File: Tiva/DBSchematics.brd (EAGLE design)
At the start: 125 x 84.1 mm, 68 parts, among them IC1 LM1117-3.3, IC2 7805T, IC3 MCP23017SO, Q1 BSS138, Q2 BSS138, U1 FT232RL, U2 LMV358, U3 LMV324, Y1 16MHz, Y2 32.768kHz

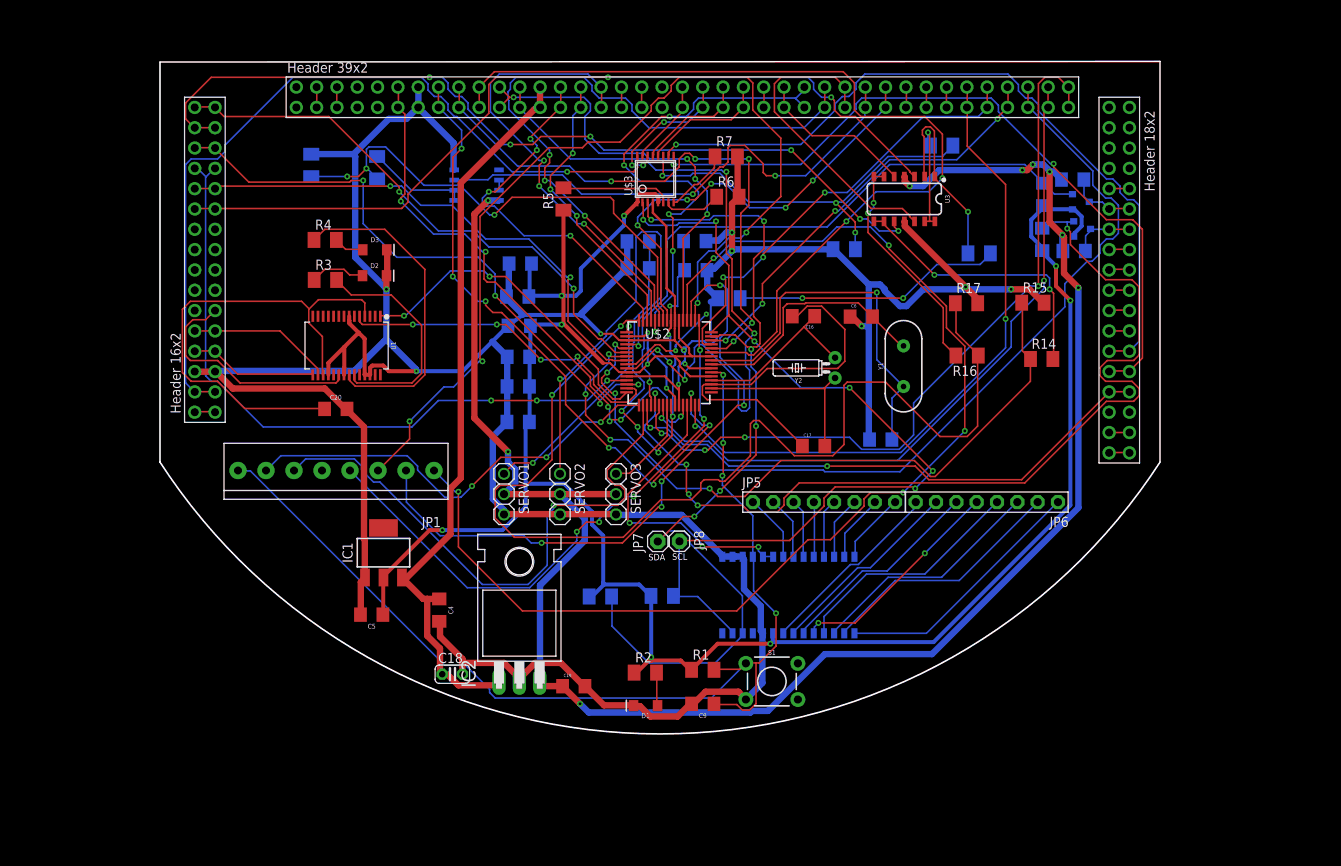
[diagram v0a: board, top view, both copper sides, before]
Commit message: uC based Board with manual Routing
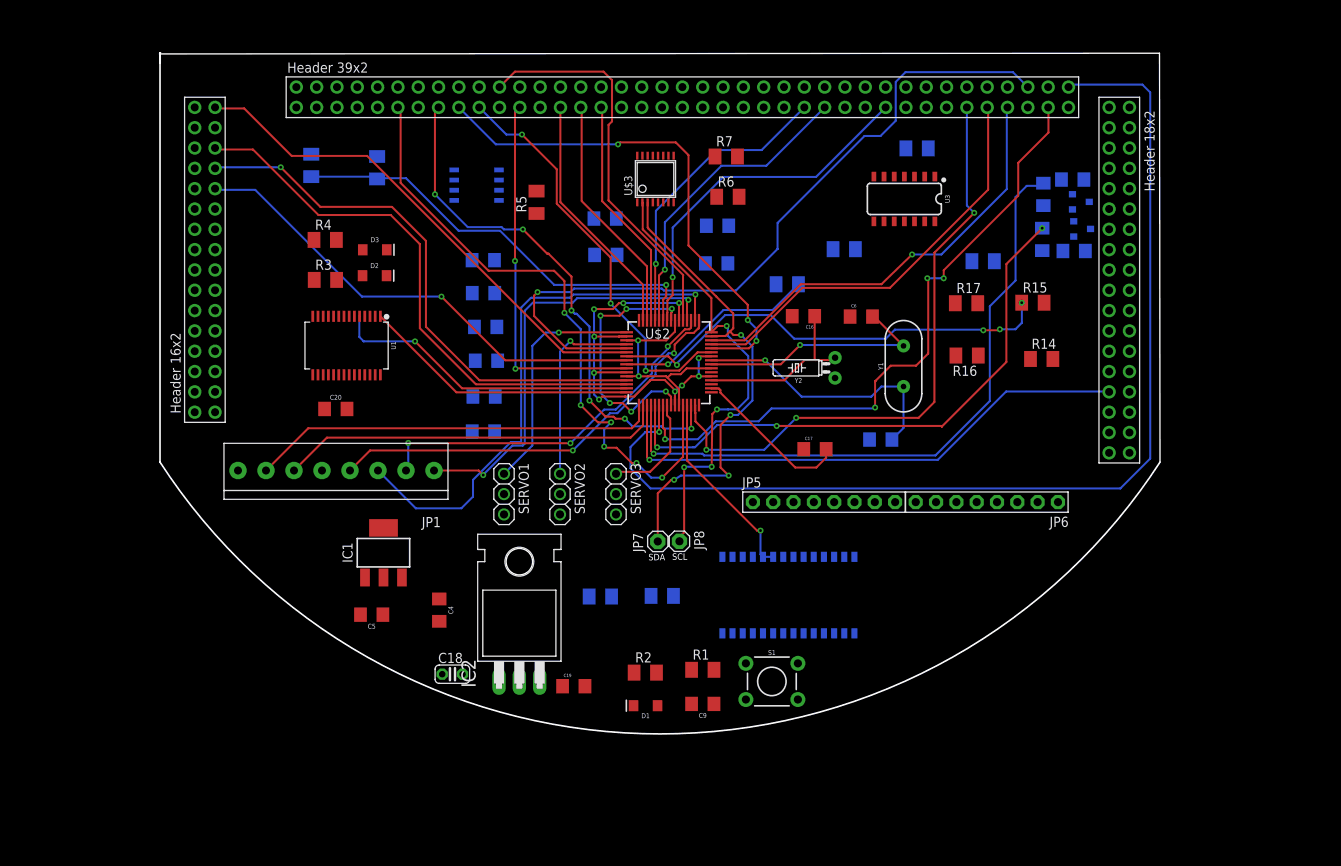
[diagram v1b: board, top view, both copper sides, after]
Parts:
- moved R13 7.50 mm to (78.4, 22.2)
- moved C1 5.02 mm to (55.6, 30.4)
- moved C11 4.64 mm to (40.4, 25.2)
- moved C8 4.50 mm to (40.4, 3.83)
- moved C14 4.45 mm to (40.5, 8.20)
- moved C2 4.36 mm to (55.7, 25.9)
- moved C7 4.29 mm to (40.4, 21.1)
- moved C12 4.20 mm to (40.7, 16.9)
- moved C13 4.02 mm to (40.8, 12.7)
- moved C10 3.43 mm to (69.7, 29.5)
- moved R5 3.39 mm to (47.1, 32.5)
- moved R18 3.10 mm to (94.6, 39.2)
- moved C3 2.74 mm to (69.6, 24.8)
- moved R12 1.09 mm to (102.9, 25.1)
- moved C17 0.44 mm to (81.9, 1.61)
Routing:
- net GND: track 496.3 -> 27.6 mm, vias 11 -> 2
- net VDD: track 295.4 -> 55.1 mm, vias 11 -> 10
- net VSERVO: track 230.0 -> 0.00 mm, vias 9 -> 0
- net N$4: track 175.0 -> 0.06 mm
- net RST: track 135.6 -> 0.00 mm, vias 4 -> 0
- net PD3: track 135.3 -> 0.00 mm, vias 2 -> 0
- net SHARP2: track 107.7 -> 0.00 mm, vias 6 -> 0
- net SHARP1: track 105.9 -> 0.00 mm, vias 2 -> 0
- net IR8: track 100.5 -> 0.00 mm, vias 1 -> 0
- net N$11: track 148.3 -> 53.7 mm, vias 5 -> 2
- net N$16: track 93.8 -> 0.00 mm, vias 1 -> 0
- net VBATTERY: track 93.0 -> 0.00 mm
- net N$7: track 92.1 -> 0.00 mm, vias 2 -> 0
- net SHARP5: track 65.2 -> 0.00 mm, vias 2 -> 0
- net N$77: track 62.5 -> 0.00 mm
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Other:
- board size 125 x 84.1 mm -> 125.1 x 85.1 mm

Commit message: Interrupt of Port Expander Added
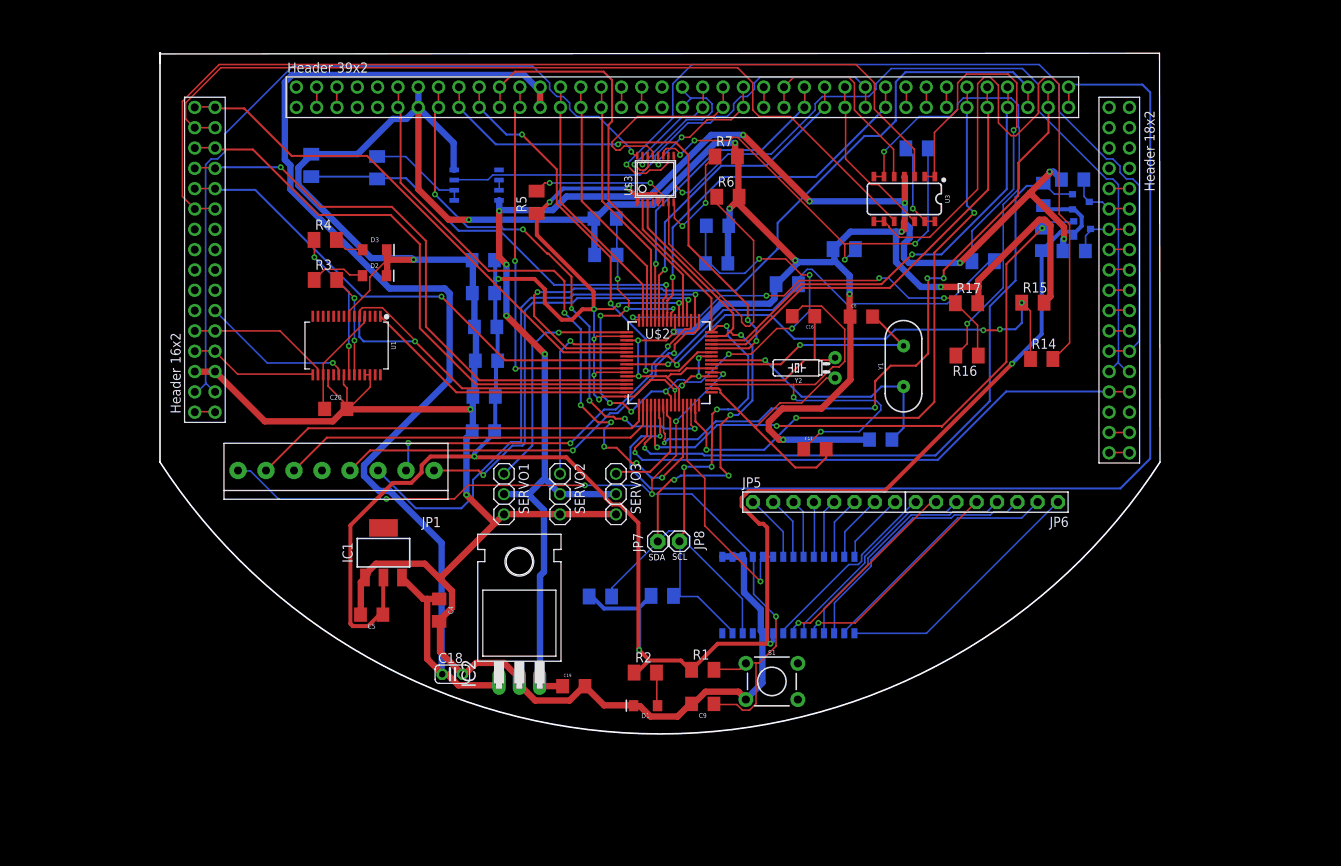
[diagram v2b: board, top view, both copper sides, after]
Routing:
- net GND: track 27.6 -> 518.0 mm, vias 2 -> 14
- net VDD: track 55.1 -> 339.1 mm, vias 10 -> 17
- net VSERVO: track 0.00 -> 183.4 mm, vias 0 -> 10
- net VBATTERY: track 0.00 -> 155.2 mm
- net RST: track 0.00 -> 123.0 mm, vias 0 -> 6
- net SHARP1: track 0.00 -> 119.8 mm
- net N$16: track 0.00 -> 111.5 mm, vias 0 -> 1
- net SHARP2: track 0.00 -> 106.6 mm
- net N$7: track 0.00 -> 100.6 mm, vias 0 -> 1
- net IR8: track 0.00 -> 96.9 mm, vias 0 -> 1
- net SDFSDFSD: track 0.00 -> 87.2 mm
- net SHARP5: track 0.00 -> 61.0 mm
- net XXVX: track 0.00 -> 59.3 mm, vias 0 -> 2
- net VDDC: track 32.6 -> 91.8 mm, vias 6 -> 11
- net EXTSHARP: track 0.00 -> 55.5 mm, vias 0 -> 4
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
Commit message: Layout Complete
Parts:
- added 3.3V, 5V, GND: (no value), adafruit:1X01
- added JP9: GND, adafruit:1X01
- moved IC2 6.48 mm to (42.7, -23.4), turned to 180 degrees
- moved C18 2.26 mm to (38.1, -24.9)
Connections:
- net GND: now also GND.1, JP1.4, JP9.1
- net VDD: now also 3.3V.1
- net VSERVO: now also 5V.1
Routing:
- net GND: track 518.0 -> 664.4 mm, vias 14 -> 53
- net VDD: track 339.1 -> 367.3 mm
- net VSERVO: track 183.4 -> 200.6 mm, vias 10 -> 11
- net VBATTERY: track 155.2 -> 162.4 mm
- added copper zone on layer 1, net GND
- added copper zone on layer 16, net GND

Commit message: final
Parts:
- moved C18 6.79 mm to (31.5, -23.7)
- moved C4 3.57 mm to (31.4, -19.1), turned to 0 degrees
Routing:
- net GND: track 664.4 -> 656.6 mm
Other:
- board text added: "1"
- board text added: "16"
- board text added: "17a"
- board text added: "17b"
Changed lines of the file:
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@@
 <wire x1="0" y1="49.93" x2="0" y2="51.097" width="0.254" layer="20"/>
 <wire x1="0" y1="51.097" x2="0.049" y2="51.146" width="0.254" layer="20"/>
+<text x="6.5" y="3.27" size="1.4224" layer="1">1</text>
+<text x="6.68" y="3.18" size="1.4224" layer="1">1</text>
+<text x="6.64" y="3.32" size="1.4224" layer="1">1</text>
+<text x="6.73" y="3.09" size="1.4224" layer="1">1</text>
+<text x="6.73" y="3.09" size="1.4224" layer="1">1</text>
+<text x="6.73" y="3.09" size="1.4224" layer="1">1</text>
+<text x="6.46" y="3" size="1.4224" layer="1">1</text>
+<text x="6.46" y="3" size="1.4224" layer="1">1</text>
+<text x="6.46" y="3" size="1.4224" layer="1">1</text>
+<text x="6.59" y="3.18" size="1.4224" layer="25">1</text>
+<text x="5.96" y="45.92" size="1.4224" layer="25">16</text>
+<text x="12.42" y="43.45" size="1.4224" layer="25">17a</text>
+<text x="12.33" y="46.01" size="1.4224" layer="25">17b</text>
 </plain>
 <attributes>
@@
 <attribute name="PROD_ID" value="CAP-10009" x="81.871" y="1.611" size="1.778" layer="27" display="off"/>
 </element>
-<element name="C18" library="adafruit" package="C025-024X044" value="100uF" x="38.145" y="-24.909"/>
+<element name="C18" library="adafruit" package="C025-024X044" value="100uF" x="31.465" y="-23.679"/>
 <element name="C19" library="SparkFun-Retired" package="1206" value="0.1uF" x="51.72" y="-28.01">
 <attribute name="PROD_ID" value="CAP-10009" x="51.72" y="-28.01" size="1.778" layer="27" display="off"/>
@@
 <attribute name="PROD_ID" value="CAP-10009" x="69.581" y="24.839" size="1.778" layer="28" rot="MR180" display="off"/>
 </element>
-<element name="C4" library="SparkFun-Capacitors" package="1206" value="10uF" x="34.905" y="-18.503" rot="R270">
-<attribute name="PROD_ID" value="CAP-10057" x="34.905" y="-18.503" size="1.778" layer="27" rot="R270" display="off"/>
+<element name="C4" library="SparkFun-Capacitors" package="1206" value="10uF" x="31.383" y="-19.085">
+<attribute name="PROD_ID" value="CAP-10057" x="31.383" y="-19.085" size="1.778" layer="27" display="off"/>
 </element>
 <element name="C5" library="SparkFun-Capacitors" package="1206" value="10uF" x="26.46" y="-19.069" rot="R180">
@@
 <wire x1="25.1" y1="-19" x2="25.06" y2="-19.069" width="0.8" layer="1"/>
 <wire x1="25.6" y1="-14.5" x2="25.623" y2="-14.423" width="0.8" layer="1"/>
-<wire x1="35" y1="-20" x2="35" y2="-23.7" width="0.8" layer="1"/>
-<wire x1="35" y1="-20" x2="34.905" y2="-19.903" width="0.8" layer="1"/>
 <wire x1="25.9" y1="-13.8" x2="25.9" y2="-14.1" width="0.8" layer="1"/>
-<wire x1="36.5" y1="-16.1" x2="34.95" y2="-14.55" width="0.8" layer="1"/>
-<wire x1="36.5" y1="-18.2" x2="36.5" y2="-16.1" width="0.8" layer="1"/>
-<wire x1="35.1" y1="-19.6" x2="36.5" y2="-18.2" width="0.8" layer="1"/>
 <wire x1="25.9" y1="-14.1" x2="25.623" y2="-14.423" width="0.8" layer="1"/>
-<wire x1="35.1" y1="-19.6" x2="34.905" y2="-19.903" width="0.8" layer="1"/>
 <wire x1="34.95" y1="-14.55" x2="42.7" y2="-6.8" width="0.8" layer="1"/>
 <wire x1="42.7" y1="-6.8" x2="43" y2="-6.54" width="0.8" layer="1"/>
@@
 <wire x1="40.7" y1="-6.5" x2="43" y2="-6.5" width="0.8128" layer="1"/>
 <wire x1="36.32923125" y1="-23.5914" x2="37.42076875" y2="-23.5914" width="0.8128" layer="1"/>
-<wire x1="35" y1="-23.7" x2="36.22063125" y2="-23.7" width="0.8128" layer="1"/>
 <wire x1="36.22063125" y1="-23.7" x2="36.32923125" y2="-23.5914" width="0.8128" layer="1"/>
-<wire x1="38.73836875" y1="-24.909" x2="39.415" y2="-24.909" width="0.8128" layer="1"/>
 <wire x1="37.42076875" y1="-23.5914" x2="38.73836875" y2="-24.909" width="0.8128" layer="1"/>
 <wire x1="66.8381" y1="-20.9783" x2="68.3783" y2="-20.9783" width="0.8128" layer="1"/>
@@
 <wire x1="63.5378" y1="-6.2922" x2="63.63" y2="-6.2" width="0.6096" layer="16"/>
 <via x="63.63" y="-6.2" extent="1-16" drill="0.3"/>
+<wire x1="32.735" y1="-23.679" x2="32.735" y2="-19.133" width="0.8128" layer="1"/>
+<wire x1="32.735" y1="-19.133" x2="32.783" y2="-19.085" width="0.8128" layer="1"/>
 </signal>
 <signal name="USB+">
@@
 <wire x1="27.4" y1="-3.6" x2="25.5" y2="-1.7" width="0.8" layer="16"/>
 <wire x1="28.7" y1="-3.6" x2="27.4" y2="-3.6" width="0.8" layer="16"/>
-<wire x1="28.7" y1="-3.6" x2="35.2" y2="-10.1" width="0.8" layer="16"/>
+<wire x1="35.2" y1="-10.1" x2="28.7" y2="-3.6" width="0.8" layer="16"/>
 <wire x1="47.5" y1="46.9" x2="47.52" y2="46.88" width="0.8" layer="16"/>
-<wire x1="36.875" y1="-24.909" x2="36.491" y2="-24.909" width="0.8128" layer="16"/>
-<wire x1="35.2" y1="-10.1" x2="36.875" y2="-11.775" width="0.8128" layer="16"/>
-<wire x1="36.875" y1="-21.336" x2="36.875" y2="-11.775" width="0.8128" layer="16"/>
-<wire x1="36.875" y1="-21.336" x2="36.875" y2="-24.909" width="0.8128" layer="16"/>
-<wire x1="30.245" y1="-14.423" x2="32.925" y2="-17.103" width="0.8128" layer="1"/>
-<wire x1="32.925" y1="-17.103" x2="34.905" y2="-17.103" width="0.8128" layer="1"/>
-<wire x1="34.905" y1="-17.103" x2="32.8" y2="-19.208" width="0.8128" layer="1"/>
-<wire x1="32.8" y1="-22.93231875" x2="34.58048125" y2="-24.7128" width="0.8128" layer="1"/>
-<wire x1="36.6788" y1="-24.7128" x2="36.875" y2="-24.909" width="0.8128" layer="1"/>
-<wire x1="32.8" y1="-19.208" x2="32.8" y2="-22.93231875" width="0.8128" layer="1"/>
-<wire x1="34.58048125" y1="-24.7128" x2="36.6788" y2="-24.7128" width="0.8128" layer="1"/>
-<wire x1="45.252" y1="-13.208" x2="45.252" y2="-17.486" width="0.8128" layer="16"/>
-<wire x1="45.252" y1="-17.486" x2="41.656" y2="-21.082" width="0.8128" layer="16"/>
-<wire x1="41.656" y1="-21.082" x2="37.129" y2="-21.082" width="0.8128" layer="16"/>
-<wire x1="37.129" y1="-21.082" x2="36.875" y2="-21.336" width="0.8128" layer="16"/>
+<wire x1="30.195" y1="-23.679" x2="30.195" y2="-19.297" width="0.8128" layer="1"/>
+<wire x1="29.983" y1="-19.085" x2="29.983" y2="-14.685" width="0.8128" layer="1"/>
+<wire x1="29.983" y1="-14.685" x2="30.245" y2="-14.423" width="0.8128" layer="1"/>
+<wire x1="44.1566" y1="-14.644575" x2="44.1566" y2="-14.3034" width="0.8128" layer="1"/>
+<wire x1="44.1566" y1="-14.3034" x2="45.252" y2="-13.208" width="0.8128" layer="1"/>
+<wire x1="30.245" y1="-14.423" x2="33.39973125" y2="-14.423" width="0.8128" layer="1"/>
+<wire x1="33.39973125" y1="-14.423" x2="34.53313125" y2="-15.5564" width="0.8128" layer="1"/>
+<wire x1="34.53313125" y1="-15.5564" x2="43.244775" y2="-15.5564" width="0.8128" layer="1"/>
+<wire x1="43.244775" y1="-15.5564" x2="44.1566" y2="-14.644575" width="0.8128" layer="1"/>
+<wire x1="45.252" y1="-17.718" x2="44.23" y2="-18.74" width="0.8128" layer="16"/>
+<wire x1="44.23" y1="-18.74" x2="38.91" y2="-18.74" width="0.8128" layer="16"/>
+<wire x1="38.91" y1="-18.74" x2="36.98" y2="-16.81" width="0.8128" layer="16"/>
+<wire x1="36.98" y1="-16.81" x2="36.98" y2="-11.88" width="0.8128" layer="16"/>
+<wire x1="45.252" y1="-13.208" x2="45.252" y2="-17.718" width="0.8128" layer="16"/>
+<wire x1="36.98" y1="-11.88" x2="35.2" y2="-10.1" width="0.8128" layer="16"/>
+<wire x1="30.195" y1="-19.297" x2="29.983" y2="-19.085" width="0" layer="19" extent="1-1"/>
 </signal>
 <signal name="WL2">

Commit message: Manual Updated
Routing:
- net TXD: track 48.3 -> 38.4 mm, vias 1 -> 0
- net GND: track 656.6 -> 653.3 mm, vias 53 -> 48
- net VDD: track 367.3 -> 369.6 mm
- net PA6: track 85.4 -> 86.5 mm
- net N$25: track 67.0 -> 67.8 mm
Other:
- outline, holes or cut-outs redrawn
- board text removed: "1"
- board text removed: "16"
- board text removed: "17a"
- board text removed: "17b"
